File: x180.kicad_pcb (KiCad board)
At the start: 6 copper layers, 50 x 50 mm, 77 parts, among them J1 U180 Header, J2 Conn_01x06_Pin, U1 ATF1502AS-7A, U2 ADG734, U3 ADG734, U4 ADG734, U5 ADG734

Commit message: Minor improvements on routing
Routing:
- net GND: track 71.2 -> 65.9 mm
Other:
- outline, holes or cut-outs redrawn
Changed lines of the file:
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@@
 	(gr_poly
 		(pts
-			(xy 47.6113 94.4744) (xy 68.657614 94.4744) (xy 85.4456 77.724) (xy 97.608 77.724) (xy 97.608 44.46737)
+			(xy 47.6113 94.4674) (xy 68.66463 94.4674) (xy 85.4456 77.724) (xy 97.6113 77.724) (xy 97.6113 44.46737)
 			(xy 58.695227 44.468015) (xy 56.06507 47.325236) (xy 47.6113 47.315972)
 		)
@@
 		(layer "Dwgs.User")
 		(pts
-			(xy 68.657614 94.4744) (xy 97.608 44.46737)
+			(xy 68.66463 94.4674) (xy 97.6113 44.46737)
 		)
 		(height 36.373255)
@@
 			(keep_text_aligned yes)
 		)
-		(gr_text "50,007"
-			(at 103.880869 69.470885 90)
+		(gr_text "50"
+			(at 103.887885 69.467385 90)
 			(layer "Dwgs.User")
 			(effects
@@
 		(layer "Dwgs.User")
 		(pts
-			(xy 97.608 44.46737) (xy 47.6113 47.315972)
+			(xy 97.6113 44.46737) (xy 47.6113 47.315972)
 		)
 		(height -7.723576)
@@
 			(keep_text_aligned yes)
 		)
-		(gr_text "49,9967"
-			(at 72.60965 35.593794 0)
+		(gr_text "50"
+			(at 72.6113 35.593794 0)
 			(layer "Dwgs.User")
 			(effects
@@
 	)
 	(segment
-		(start 70.2818 62.1538)
-		(end 70.2818 62.3062)
+		(start 70.4088 62.1538)
+		(end 70.6628 62.4078)
 		(width 0.25)
 		(layer "B.Cu")
@@
 	)
 	(segment
-		(start 70.2818 62.3062)
-		(end 70.3834 62.4078)
+		(start 73.2295 62.4078)
+		(end 73.3823 62.255)
 		(width 0.25)
 		(layer "B.Cu")
@@
 	)
 	(segment
-		(start 70.3834 62.4078)
-		(end 73.2295 62.4078)
+		(start 70.2818 62.1538)
+		(end 70.4088 62.1538)
 		(width 0.25)
 		(layer "B.Cu")
@@
 	)
 	(segment
-		(start 73.2295 62.4078)
-		(end 73.3823 62.255)
+		(start 70.6628 62.4078)
+		(end 73.2295 62.4078)
 		(width 0.25)
 		(layer "B.Cu")
@@
 	)
 	(segment
-		(start 63.6524 67.437)
-		(end 65.7352 65.3542)
+		(start 61.2648 67.437)
+		(end 63.6524 67.437)
 		(width 0.25)
 		(layer "F.Cu")
@@
 	)
 	(segment
-		(start 59.8835 66.4464)
-		(end 60.2742 66.4464)
+		(start 58.7629 61.976)
+		(end 57.44485 60.65795)
 		(width 0.25)
 		(layer "F.Cu")
@@
 	)
 	(segment
-		(start 59.39485 62.484)
-		(end 59.1058 62.484)
+		(start 68.8818 60.1502)
+		(end 68.8818 59.051013)
 		(width 0.25)
 		(layer "F.Cu")
@@
 	)
 	(segment
-		(start 57.44485 60.82305)
-		(end 57.44485 59.3675)
+		(start 68.7324 60.2996)
+		(end 68.8818 60.1502)
 		(width 0.25)
 		(layer "F.Cu")
@@
 	)
 	(segment
-		(start 68.8818 59.7438)
-		(end 68.8818 59.051013)
+		(start 57.9374 63.754)
+		(end 59.39485 63.754)
 		(width 0.25)
 		(layer "F.Cu")
@@
 	)
 	(segment
-		(start 58.2676 63.4238)
-		(end 59.39485 63.4238)
+		(start 59.39485 59.3675)
+		(end 59.39485 65.0925)
 		(width 0.25)
 		(layer "F.Cu")
@@
 	)
 	(segment
-		(start 59.39485 59.3675)
-		(end 59.39485 65.0925)
+		(start 57.44485 64.24655)
+		(end 57.9374 63.754)
 		(width 0.25)
 		(layer "F.Cu")
@@
 	)
 	(segment
-		(start 59.39485 65.95775)
-		(end 59.8835 66.4464)
+		(start 66.802 65.3542)
+		(end 67.6148 64.5414)
 		(width 0.25)
 		(layer "F.Cu")
@@
 	)
 	(segment
-		(start 59.1058 62.484)
-		(end 57.44485 60.82305)
+		(start 67.6148 64.5414)
+		(end 67.6148 61.0108)
 		(width 0.25)
 		(layer "F.Cu")
@@
 	)
 	(segment
-		(start 57.44485 64.24655)
-		(end 58.2676 63.4238)
+		(start 57.44485 65.0925)
+		(end 57.44485 64.24655)
 		(width 0.25)
 		(layer "F.Cu")
@@
 	)
 	(segment
-		(start 65.7352 65.3542)
-		(end 66.802 65.3542)
+		(start 67.6148 61.0108)
+		(end 68.326 60.2996)
 		(width 0.25)
 		(layer "F.Cu")
@@
 	)
 	(segment
-		(start 57.44485 65.0925)
-		(end 57.44485 64.24655)
+		(start 63.6524 67.437)
+		(end 65.7352 65.3542)
 		(width 0.25)
 		(layer "F.Cu")
@@
 	)
 	(segment
-		(start 67.6148 64.5414)
-		(end 67.6148 61.0108)
+		(start 68.326 60.2996)
+		(end 68.7324 60.2996)
+		(width 0.25)
+		(layer "F.Cu")
+		(net 26)
+	)
+	(segment
+		(start 57.44485 60.65795)
+		(end 57.44485 59.3675)
+		(width 0.25)
+		(layer "F.Cu")
+		(net 26)
+	)
+	(segment
+		(start 65.7352 65.3542)
+		(end 66.802 65.3542)
 		(width 0.25)
 		(layer "F.Cu")
@@
 	)
 	(segment
-		(start 66.802 65.3542)
-		(end 67.6148 64.5414)
+		(start 59.8835 66.4464)
+		(end 60.2742 66.4464)
 		(width 0.25)
 		(layer "F.Cu")
@@
 	)
 	(segment
-		(start 61.2648 67.437)
-		(end 63.6524 67.437)
+		(start 59.39485 65.95775)
+		(end 59.8835 66.4464)
 		(width 0.25)
 		(layer "F.Cu")
@@
 	)
 	(segment
-		(start 67.6148 61.0108)
-		(end 68.8818 59.7438)
+		(start 59.39485 61.976)
+		(end 58.7629 61.976)
 		(width 0.25)
 		(layer "F.Cu")
@@
 	)
 	(segment
-		(start 75.2856 58.8518)
-		(end 75.7936 58.8518)
-		(width 0.4)
-		(layer "In3.Cu")
-		(net 37)
-	)
-	(segment
-		(start 75.7936 58.8518)
-		(end 79.1972 62.2554)
-		(width 0.4)
-		(layer "In3.Cu")
-		(net 37)
-	)
-	(segment
 		(start 58.09485 59.3675)
 		(end 58.09485 60.2742)
@@
 	)
 	(segment
-		(start 88.4955 73.66)
-		(end 85.7231 73.66)
-		(width 1)
-		(layer "F.Cu")
-		(net 55)
-	)
-	(segment
 		(start 77.5716 70.280813)
 		(end 79.0418 71.751013)
@@
 	)
 	(segment
-		(start 85.7231 73.66)
-		(end 85.5726 73.5095)
-		(width 1)
-		(layer "F.Cu")
-		(net 55)
-	)
-	(segment
 		(start 81.7626 73.5095)
 		(end 85.5726 73.5095)
@@
 	)
 	(segment
+		(start 88.4955 73.66)
+		(end 88.345 73.5095)
+		(width 1)
+		(layer "F.Cu")
+		(net 55)
+	)
+	(segment
 		(start 78.0561 67.2065)
 		(end 77.5716 67.691)
@@
 		(layer "F.Cu")
 		(net 55)
+	)
+	(segment
+		(start 88.345 73.5095)
+		(end 85.5726 73.5095)
+		(width 1)
+		(layer "F.Cu")
+		(net 55)

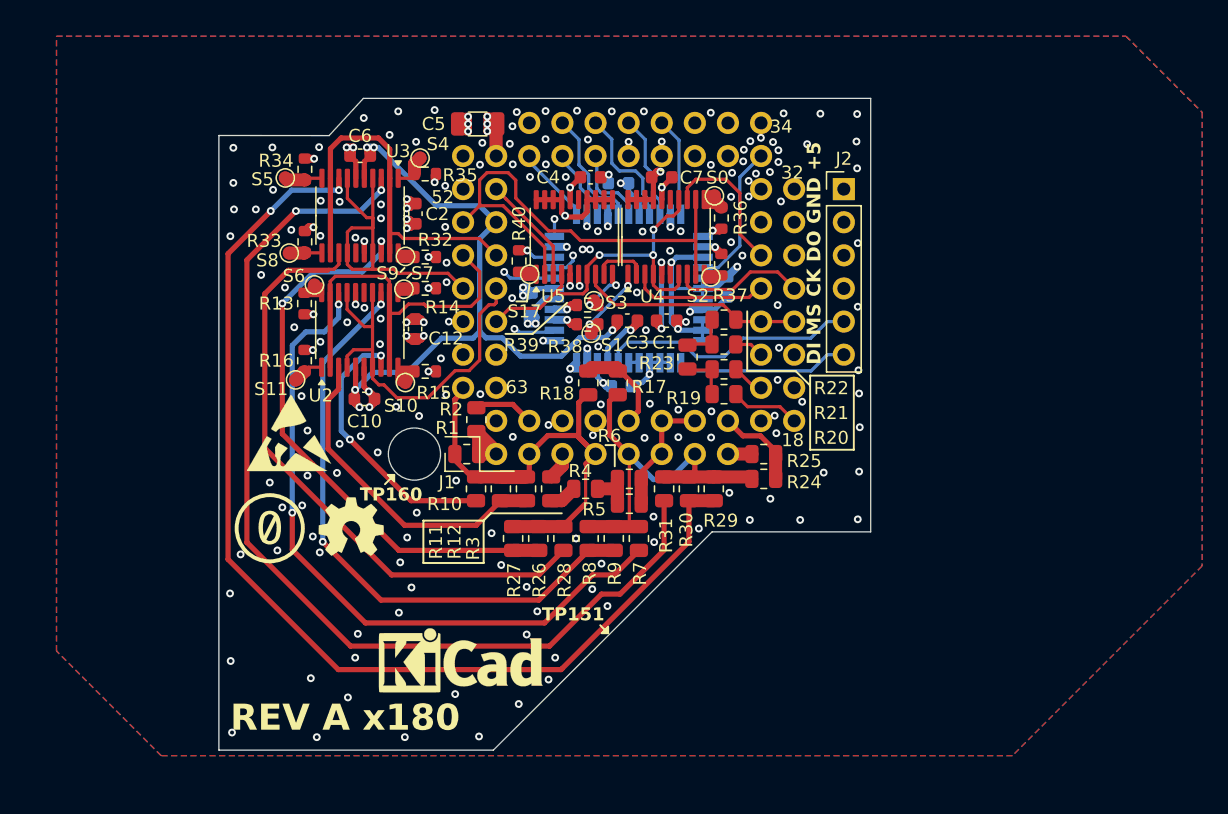
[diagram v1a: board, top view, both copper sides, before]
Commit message: REV B: redesign with resistor networks
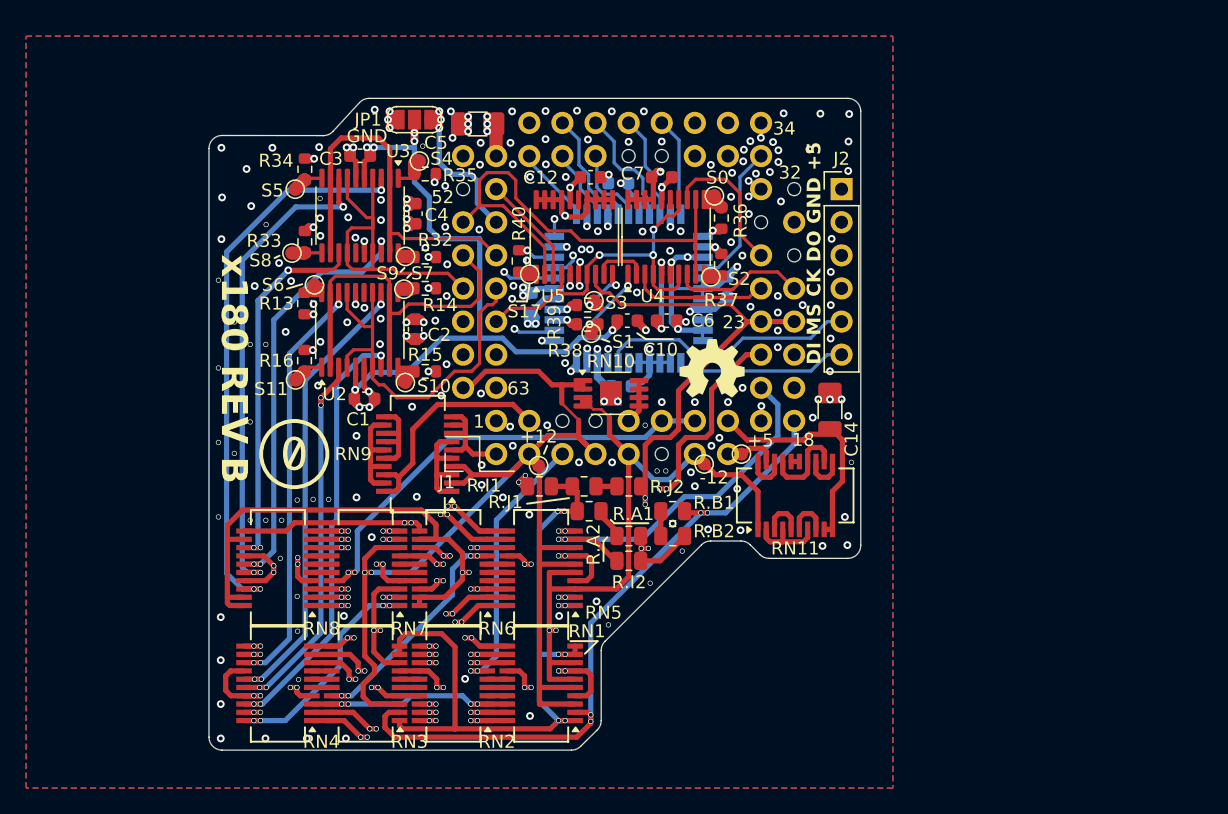
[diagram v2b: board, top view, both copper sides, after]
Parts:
- removed R1: 4k3, Resistor_SMD:R_0805_2012Metric
- removed R10, R28, R3, R31, R4, R5, R6, R7: 20k, Resistor_SMD:R_0805_2012Metric
- removed R11, R12, R26, R27, R29, R30, R8, R9: 160k, Resistor_SMD:R_0805_2012Metric
- removed R17, R18, R25: 10k, Resistor_SMD:R_0805_2012Metric
- removed R19, R22, R23: 37k5, Resistor_SMD:R_0805_2012Metric
- removed R2: 6k2, Resistor_SMD:R_0805_2012Metric
- removed R20, R21: 16k7, Resistor_SMD:R_0805_2012Metric
- removed R24: 24k, Resistor_SMD:R_0805_2012Metric
- added +12: TestPoint_Small, MiDi:TestPoint_Pad_D1.0mm, F.Cu at (72.1, 72.6)
- added +5: TestPoint_Small, MiDi:TestPoint_Pad_D1.0mm, F.Cu at (87.7, 71.8)
- added -12: TestPoint_Small, MiDi:TestPoint_Pad_D1.0mm, F.Cu at (84.8, 72.5)
- added C14: 100n, Capacitor_SMD:C_1206_3216Metric, F.Cu at (94.5, 68.3)
- added JP1: SolderJumper_3_Open, Jumper:SolderJumper-3_P1.3mm_Open_RoundedPad1.0x1.5mm, F.Cu at (62.6, 46.1)
- added R.A1: 300k, Resistor_SMD:R_0805_2012Metric, F.Cu at (76.0, 76.1)
- added R.A2: 300k, Resistor_SMD:R_0805_2012Metric, F.Cu at (79.1, 78.0)
- added R.B1: 300k, Resistor_SMD:R_0805_2012Metric, F.Cu at (82.4, 76.1)
- added R.B2: 300k, Resistor_SMD:R_0805_2012Metric, F.Cu at (82.4, 78.0)
- added R.I1: 100k, Resistor_SMD:R_0805_2012Metric, F.Cu at (72.2, 74.2)
- added R.I2: 100k, Resistor_SMD:R_0805_2012Metric, F.Cu at (79.1, 79.9)
- added R.J1: 300k, Resistor_SMD:R_0805_2012Metric, F.Cu at (75.6, 74.2)
- added R.J2: 300k, Resistor_SMD:R_0805_2012Metric, F.Cu at (79.1, 74.2)
- added RN1: OSOP 20k, MiDi:SSOP-20_3.9x8.7mm_P0.635mm, F.Cu at (72.3, 89.3)
- added RN10: LT5400 10k, Package_SO:MSOP-8-1EP_3x3mm_P0.65mm_EP1.68x1.88mm, F.Cu at (77.7, 67.1)
- added RN11: OSOP 5k, MiDi:SSOP-20_3.9x8.7mm_P0.635mm, F.Cu at (91.8, 74.9)
- added RN2: OSOP 20k, MiDi:SSOP-20_3.9x8.7mm_P0.635mm, F.Cu at (65.6, 89.3)
- added RN3: OSOP 20k, MiDi:SSOP-20_3.9x8.7mm_P0.635mm, F.Cu at (58.9, 89.3)
- added RN4: OSOP 20k, MiDi:SSOP-20_3.9x8.7mm_P0.635mm, F.Cu at (52.1, 89.3)
- added RN5: OSOP 20k, MiDi:SSOP-20_3.9x8.7mm_P0.635mm, F.Cu at (72.3, 80.5)
- added RN6: OSOP 20k, MiDi:SSOP-20_3.9x8.7mm_P0.635mm, F.Cu at (65.6, 80.5)
- added RN7: OSOP 20k, MiDi:SSOP-20_3.9x8.7mm_P0.635mm, F.Cu at (58.9, 80.5)
- added RN8: OSOP 20k, MiDi:SSOP-20_3.9x8.7mm_P0.635mm, F.Cu at (52.1, 80.5)
- added RN9: OSOP 5k, MiDi:SSOP-20_3.9x8.7mm_P0.635mm, F.Cu at (62.9, 71.8)
- R13, R14, R15, R16, R32, R33, R34, R35, R36, R37, R38, R39, R40: value 100R -> 22R
- REF** (x2): moved to B.Cu
- moved G*** 30.2 mm to (85.4, 65.2)
- moved C6 26.7 mm to (82.0, 61.5), turned to 0 degrees
- moved C3 24.1 mm to (58.4, 48.9), turned to 180 degrees
- moved C1 24.0 mm to (58.8, 67.5)
- moved C10 21.0 mm to (78.9, 61.5)
- moved REF** 18.2 mm to (57.0, 72.4), turned to 180 degrees
- moved C12 17.8 mm to (76.1, 50.5), turned to 180 degrees
- moved REF** 15.6 mm to (54.4, 85.6), turned to 180 degrees
- moved C4 13.7 mm to (62.7, 53.3), turned to -90 degrees
- moved C2 8.86 mm to (62.7, 62.2), turned to 90 degrees
- moved REF** 5.96 mm to (70.2, 86.1)
- moved S5 1.15 mm to (53.5, 51.4)
- moved S4 0.23 mm to (63.0, 49.3)
- moved S8 0.20 mm to (53.2, 56.3)
- moved J2 0.17 mm to (95.4, 51.4)
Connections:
- C1 pad 1: GND2 -> VSS
- C10 pad 1: GND2 -> VSS
- C3 pad 1: GND2 -> VSS
- C6 pad 1: GND2 -> VSS
- J1 pad 1: (no net) -> GND
- J1 pad 17: (no net) -> GND
- J1 pad 57: PIN57 AGND1 -> AGND
- J1 pad 58: PIN58 AGND2 -> AGND
- J1 pad 59: PIN59 AGND3 -> GND
- J1 pad 60: (no net) -> GND
- J1 pad 61: (no net) -> GND
- J1 pad 62: (no net) -> GND
- U2 pad 13: Net-(U2C-D3) -> -12ref1 80k
- U2 pad 14: PIN57 AGND1 -> AGND
- U2 pad 17: PIN57 AGND1 -> AGND
- U2 pad 18: Net-(U2D-D4) -> -12ref1 20k
- U2 pad 3: Net-(U2A-D1) -> +12ref1 80k
- U2 pad 4: PIN57 AGND1 -> AGND
- U2 pad 5: GND2 -> VSS
- U2 pad 7: PIN57 AGND1 -> AGND
- U2 pad 8: Net-(U2B-D2) -> +12ref1 20k
- U3 pad 13: Net-(U3C-D3) -> +12ref2 20k
- U3 pad 14: PIN58 AGND2 -> AGND
- U3 pad 17: PIN58 AGND2 -> AGND
- U3 pad 18: Net-(U3D-D4) -> +12ref2 80k
- U3 pad 3: Net-(U3A-D1) -> -12ref2 20k
- U3 pad 4: PIN58 AGND2 -> AGND
- U3 pad 5: GND2 -> VSS
- U3 pad 7: PIN58 AGND2 -> AGND
- U3 pad 8: Net-(U3B-D2) -> -12ref2 80k
- U4 pad 14: PIN59 AGND3 -> GND
- U4 pad 4: PIN59 AGND3 -> GND
- U4 pad 5: GND2 -> VSS
- U4 pad 7: PIN59 AGND3 -> GND
- U5 pad 4: PIN59 AGND3 -> GND
- U5 pad 5: GND2 -> VSS
- U5 pad 7: PIN59 AGND3 -> GND
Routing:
- net Net-(U3B-D2): track 82.9 -> 0.00 mm, vias 2 -> 0
- net Net-(U3A-D1): track 77.2 -> 0.00 mm, vias 2 -> 0
- net VSS: track 0.00 -> 74.9 mm, vias 0 -> 10
- net PIN21 LADT1: track 2.18 -> 72.0 mm, vias 0 -> 8
- net Net-(RN6A-R1.2): track 0.00 -> 61.7 mm, vias 0 -> 4
- net -12ref2 20k: track 0.00 -> 60.8 mm, vias 0 -> 5
- net +12_REF: track 37.6 -> 96.7 mm, vias 0 -> 2
- net AGND: track 0.00 -> 58.4 mm
- net GND2: track 71.9 -> 14.2 mm, vias 8 -> 3
- net Net-(RN1A-R1.1): track 0.00 -> 54.5 mm, vias 0 -> 6
- net Net-(U2D-D4): track 53.3 -> 0.00 mm, vias 2 -> 0
- net PIN23 LAD: track 17.2 -> 69.1 mm, vias 0 -> 4
- net +12ref1 20k: track 0.00 -> 50.4 mm, vias 0 -> 5
- net Net-(RN2A-R1.2): track 0.00 -> 49.5 mm, vias 0 -> 8
- net -12ref1 20k: track 0.00 -> 48.1 mm, vias 0 -> 5
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- added copper zone on In2.Cu, net GND
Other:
- outline, holes or cut-outs redrawn
- board text added: "1"
- board text added: "23"
- board text added: "GND"
- board text added: "Michael D. 10/2025"
- board text added: "TODO REV C: RN9: move up (it touches RN6)"
- board text added: "x180 REV B"
- board text removed: "Michael D. 9/2025"
- board text removed: "REV A x180"
- board text removed: "TP151"
- board text removed: "TP160"
